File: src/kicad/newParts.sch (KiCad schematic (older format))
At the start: 6 parts, among them U12 74HC08, U2 74HC08, U2E1 74HC08, U3 74HC4511D, U4 HEF4518BT, U8 74HC08

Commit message: added sub-schemes
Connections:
- net +5V: no longer U2.14 (VCC)
- net GND: no longer U2.7 (GND)
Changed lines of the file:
@@
 $Descr A4 11693 8268
 encoding utf-8
-Sheet 2 2
+Sheet 2 6
 Title ""
 Date ""
@@
 $Comp
 L PB170:74HC08 U2
-U 5 1 5FE8D2BE
+U 2 1 5FE8D2BE
 P 4050 1450
 F 0 "U2" H 4280 1496 50  0000 L CNN
@@
 F 3 "https://datasheet.lcsc.com/szlcsc/Nexperia-74HC08D-653_C5593.pdf" H 4050 1450 50  0001 C CNN
 F 4 "C5593" H 4050 1450 50  0001 C CNN "LCSC"
-	5    4050 1450
+	2    4050 1450
 	1    0    0    -1
 $EndComp

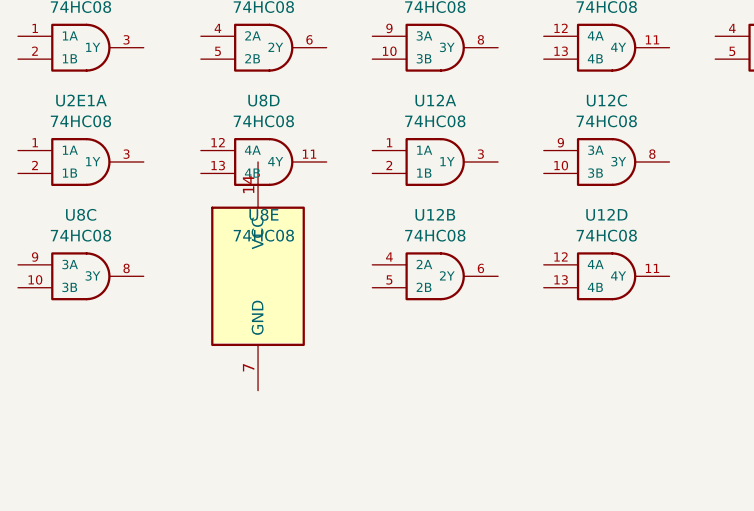
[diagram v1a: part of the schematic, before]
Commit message: added OR gates
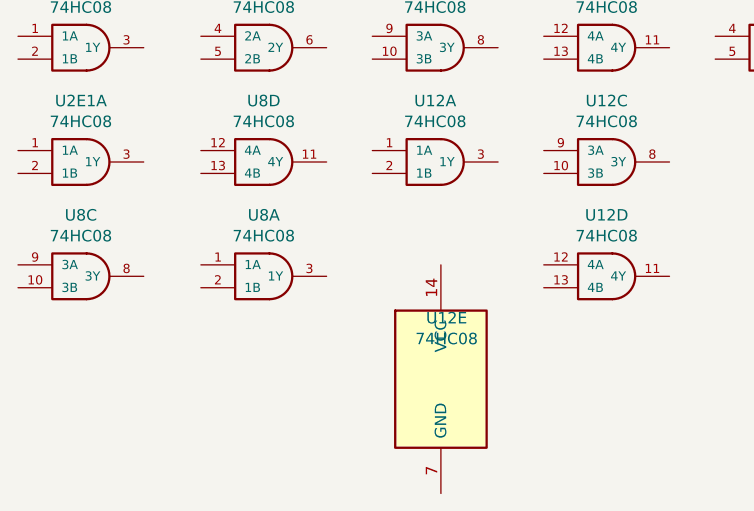
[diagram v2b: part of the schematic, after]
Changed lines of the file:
@@
 $Comp
 L PB170:74HC08 U8
-U 5 1 5FF6C8BB
+U 1 1 5FF6C8BB
 P 1800 2450
 F 0 "U8" H 1825 2717 50  0000 C CNN
@@
 F 3 "https://datasheet.lcsc.com/szlcsc/Nexperia-74HC08D-653_C5593.pdf" H 1800 2450 50  0001 C CNN
 F 4 "C5593" H 1800 2450 50  0001 C CNN "LCSC"
-	5    1800 2450
+	1    1800 2450
 	1    0    0    -1
 $EndComp
 $Comp
 L PB170:74HC08 U12
-U 2 1 5FF6C8C2
-P 2550 2450
-F 0 "U12" H 2575 2717 50  0000 C CNN
-F 1 "74HC08" H 2575 2626 50  0000 C CNN
-F 2 "Housings_SOIC:SOIC-14_3.9x8.7mm_Pitch1.27mm" H 2550 2450 50  0001 C CNN
-F 3 "https://datasheet.lcsc.com/szlcsc/Nexperia-74HC08D-653_C5593.pdf" H 2550 2450 50  0001 C CNN
-F 4 "C5593" H 2550 2450 50  0001 C CNN "LCSC"
-	2    2550 2450
+U 5 1 5FF6C8C2
+P 2600 2900
+F 0 "U12" H 2625 3167 50  0000 C CNN
+F 1 "74HC08" H 2625 3076 50  0000 C CNN
+F 2 "Housings_SOIC:SOIC-14_3.9x8.7mm_Pitch1.27mm" H 2600 2900 50  0001 C CNN
+F 3 "https://datasheet.lcsc.com/szlcsc/Nexperia-74HC08D-653_C5593.pdf" H 2600 2900 50  0001 C CNN
+F 4 "C5593" H 2600 2900 50  0001 C CNN "LCSC"
+	5    2600 2900
 	1    0    0    -1
 $EndComp

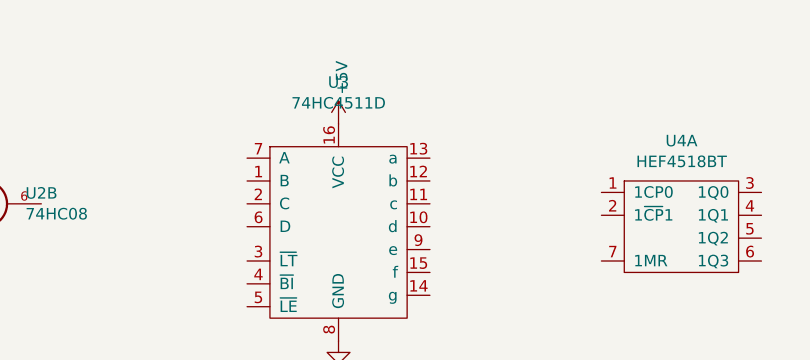
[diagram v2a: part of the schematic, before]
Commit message: added D flip flops
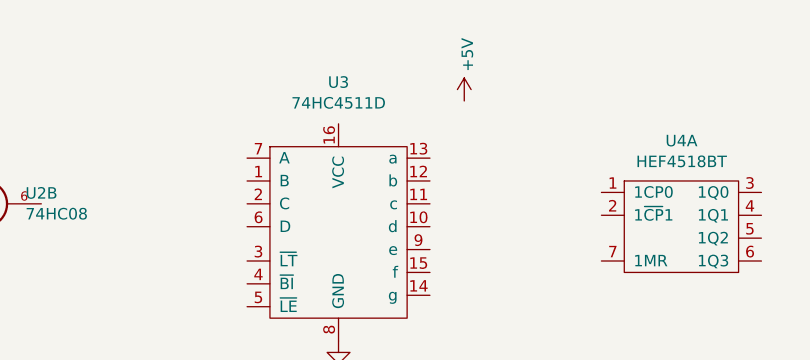
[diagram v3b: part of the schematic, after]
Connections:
- net +5V: no longer U3.16 (VCC)
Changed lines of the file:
@@
 L power:+5V #PWR?
 U 1 1 5FE90CCE
-P 5650 1100
+P 6200 1000
 AR Path="/5FE90CCE" Ref="#PWR?"  Part="1"
 AR Path="/5FEB4D4D/5FE90CCE" Ref="#PWR0127"  Part="1"
-F 0 "#PWR0127" H 5650 950 50  0001 C CNN
-F 1 "+5V" V 5665 1228 50  0000 L CNN
-F 2 "" H 5650 1100 50  0001 C CNN
-F 3 "" H 5650 1100 50  0001 C CNN
-	1    5650 1100
+F 0 "#PWR0127" H 6200 850 50  0001 C CNN
+F 1 "+5V" V 6215 1128 50  0000 L CNN
+F 2 "" H 6200 1000 50  0001 C CNN
+F 3 "" H 6200 1000 50  0001 C CNN
+	1    6200 1000
 	1    0    0    -1
 $EndComp
